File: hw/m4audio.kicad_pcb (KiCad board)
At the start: 2 copper layers, 49.7 x 49.7 mm, 91 parts, among them J1 JACK_TRS, J11 CONN_01X03, J2 JACK_TRS, J21 CONN_01X03, P1 CONN_01X02, P2 USB_OTG, P3 CONN_02X05, P4 CONN_01X08, P5 CONN_01X03, P6 CONN_01X04, U1 LD1117S33TR, U2 STM32F405RG, U3 AD8542, U4 WM8731, Y1 Crystal

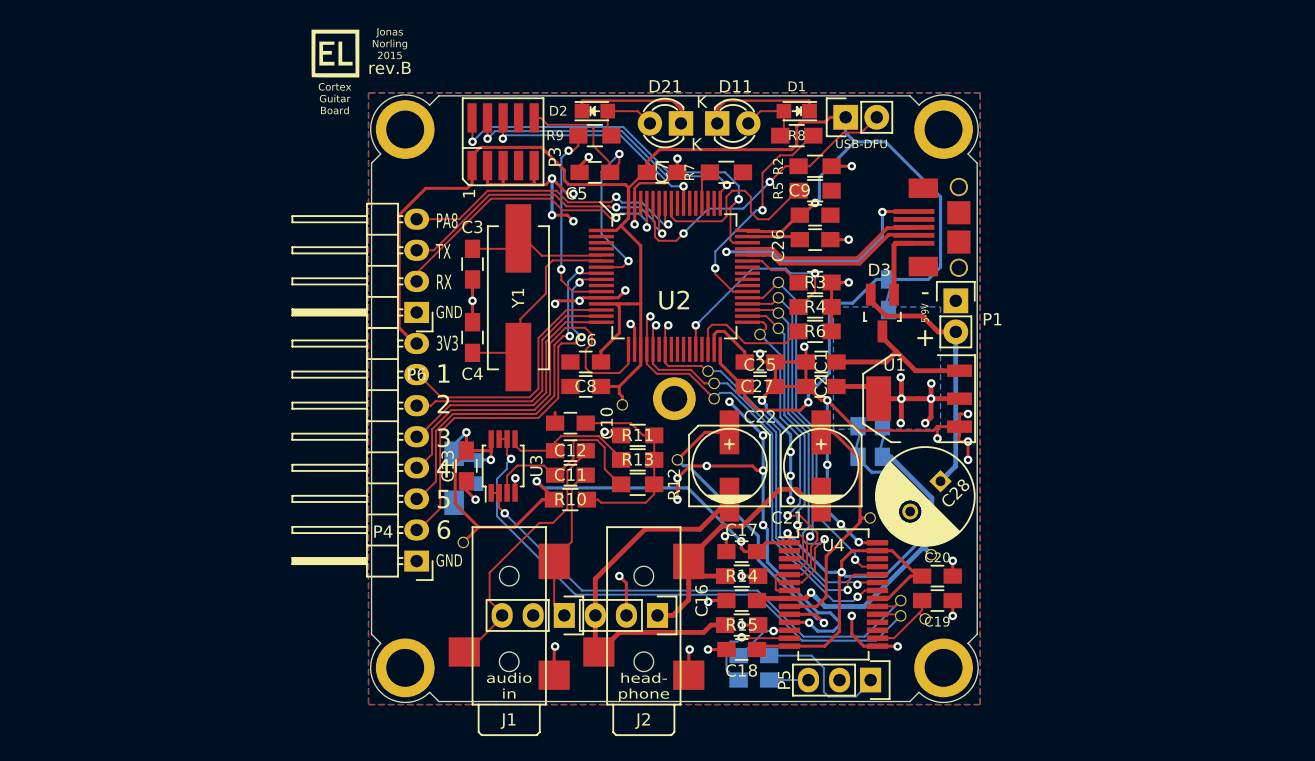
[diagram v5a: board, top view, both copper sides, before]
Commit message: Small fixes to routing, silkscreen
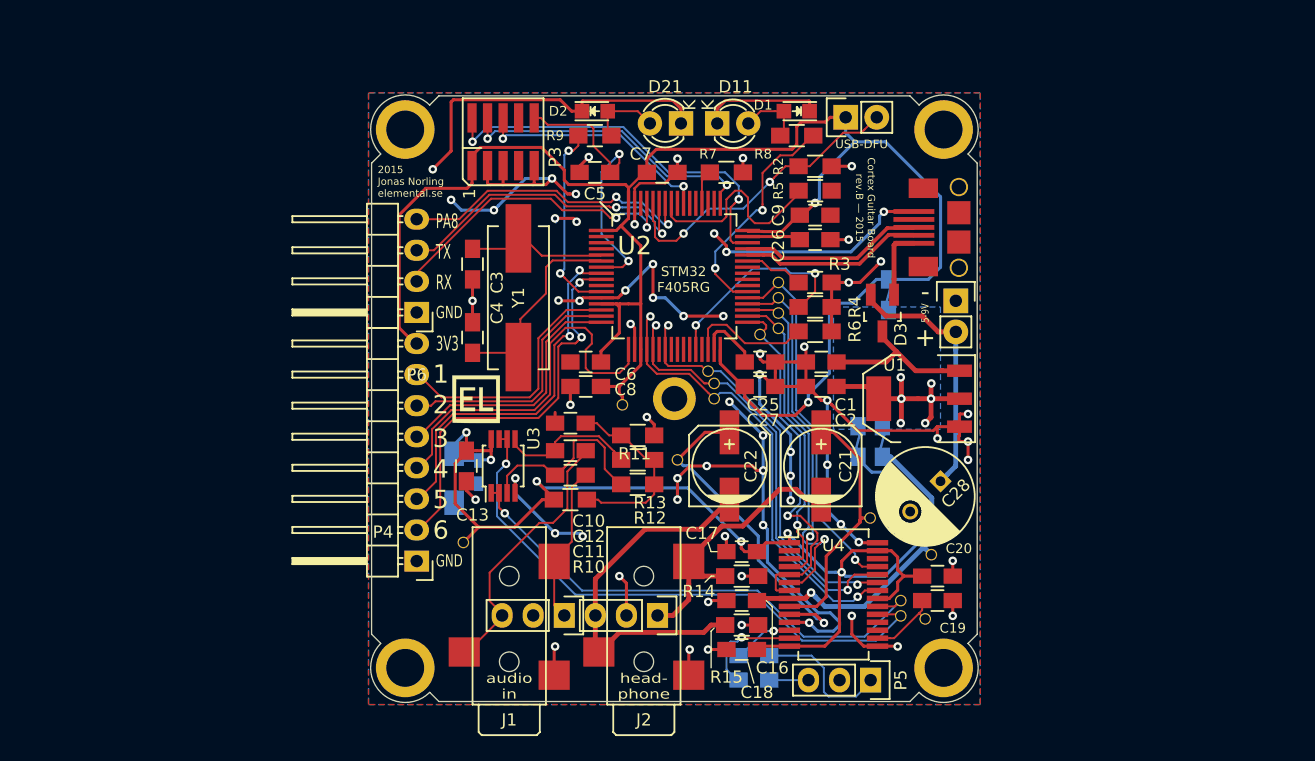
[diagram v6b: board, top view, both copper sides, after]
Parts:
- moved G*** 30.5 mm to (119.8, 115.0)
- moved OSHW 3.40 mm to (150.5, 96.0), turned to 200 degrees
- turned R11 to 180 degrees
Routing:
- net GND: track 209.4 -> 262.8 mm, vias 54 -> 67
- net /audio/bias: track 16.7 -> 15.5 mm
- net VDD: track 147.7 -> 148.2 mm
- net VAA: track 103.8 -> 103.3 mm
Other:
- board text added: "2015 Jonas Norling elemental.se"
- board text added: "BOOT0"
- board text added: "Cortex Guitar Board rev.B — 2015"
- board text added: "Cortex Guitar Board—rev.B-Jonas Norling 2015"
- board text added: "STM32 F405RG"
- board text removed: "Cortex Guitar Board"
- board text removed: "Cortex Guitar Board rev.B Jonas Norling 2015"
- board text removed: "Jonas Norling 2015"
- board text removed: "rev.B"

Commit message: Tidy up routing, add OSHW logo
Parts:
- removed OSHW: Symbol_OSHW-Logo_SilkScreen, Symbols:Symbol_OSHW-Logo_SilkScreen
- added G***: LOGO, Jonas_Gnomes:OSHW_4mm_mask, B.Cu at (143.8, 102.0)
- added G***: LOGO, elemental:elemental-4mm-mask, B.Cu at (147.8, 102.0)
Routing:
- net GND: track 262.8 -> 244.6 mm, vias 67 -> 65
- net /PWR_3V3: track 17.7 -> 20.0 mm, vias 6 -> 9
- net VAA: track 103.3 -> 105.1 mm
- net /BOOT1: track 17.7 -> 16.8 mm
- net VDD: track 148.2 -> 148.8 mm
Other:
- board text added: "elemental.se"

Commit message: Board revision B finished
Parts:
- added TP17: TST, Jonas_Connectors:TP_0.7mm, B.Cu at (128.0, 100.5)
- added TP18: TST, Jonas_Connectors:TP_0.7mm, B.Cu at (127.2, 102.5)
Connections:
- U2 pad 3: (no net) -> Net-(TP17-Pad1)
- U2 pad 4: (no net) -> Net-(TP18-Pad1)
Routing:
- net Net-(TP17-Pad1): track 0.00 -> 3.49 mm
- net Net-(TP18-Pad1): track 0.00 -> 2.63 mm
- net GND: track 244.6 -> 246.4 mm
- net VDD: track 148.8 -> 148.2 mm
